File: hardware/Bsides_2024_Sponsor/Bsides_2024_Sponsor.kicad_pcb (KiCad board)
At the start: 2 copper layers, 139.6 x 139.6 mm, 65 parts, among them J1 Serial_IN, J2 Add_On, J3 OLED, J4 Serial_OUT, J5 Battery, J6 Battery, P1 USB_C_Plug_USB2.0, Q1 DMG3415U-7, SW1 ON, SW2 RESET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

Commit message: feat(hw): logos sponsor
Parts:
- added G***: LOGO, LOGO, B.Cu at (164.9, 141.1)
- added G***: LOGO, LOGO, B.Cu at (143.4, 102.8)
- added REF**: OSHW-Logo_7.5x8mm_SilkScreen, Symbol:OSHW-Logo_7.5x8mm_SilkScreen, B.Cu at (90.1, 132.8)
- added kibuzzard-666C8E87: G***, kibuzzard-666C8E87, B.Cu at (143.5, 98.5)
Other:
- board text added: "4e6576657220676f6e6e612067 69766520796f752075700a4e65 76657220676f6e6e61206c6574 20796f7520646f776e0a4e6576 657220676f6e6e612072756e20 61726f756e6420616e64206465 7365727420796f75"
- board text added: "Aqui inicia el tour por latinoamerica Parce Wey Che"
- board text added: "Elige tu bando, rudo o tecnico?"
- board text added: "Lucharan de 2 a 3 caidas sin limite de tiempo!!"

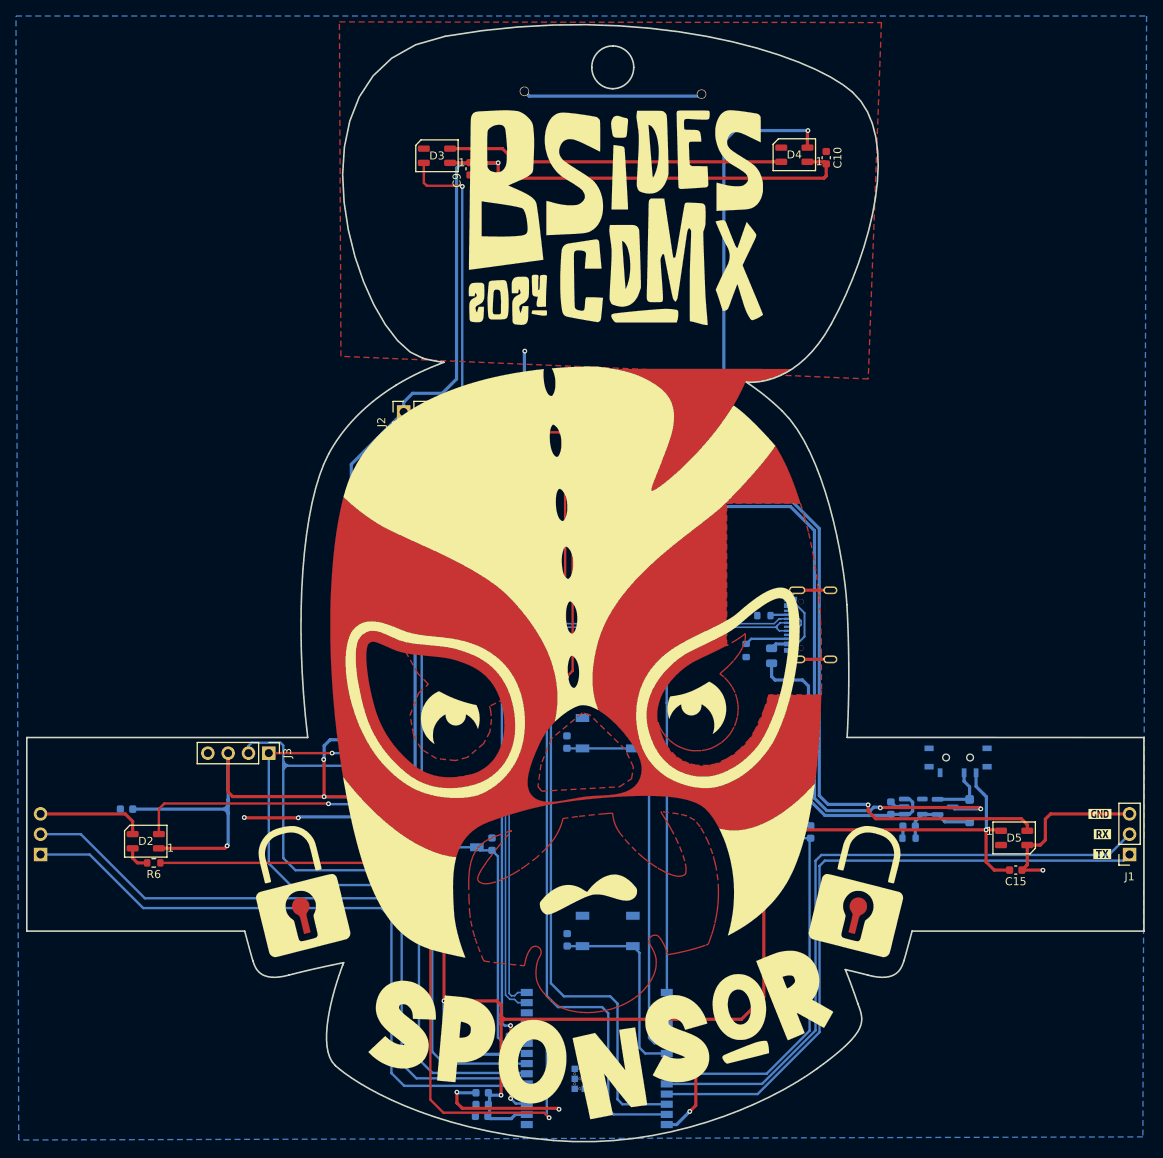
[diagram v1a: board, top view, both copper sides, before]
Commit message: feat(Hw):Update_footprint_badge
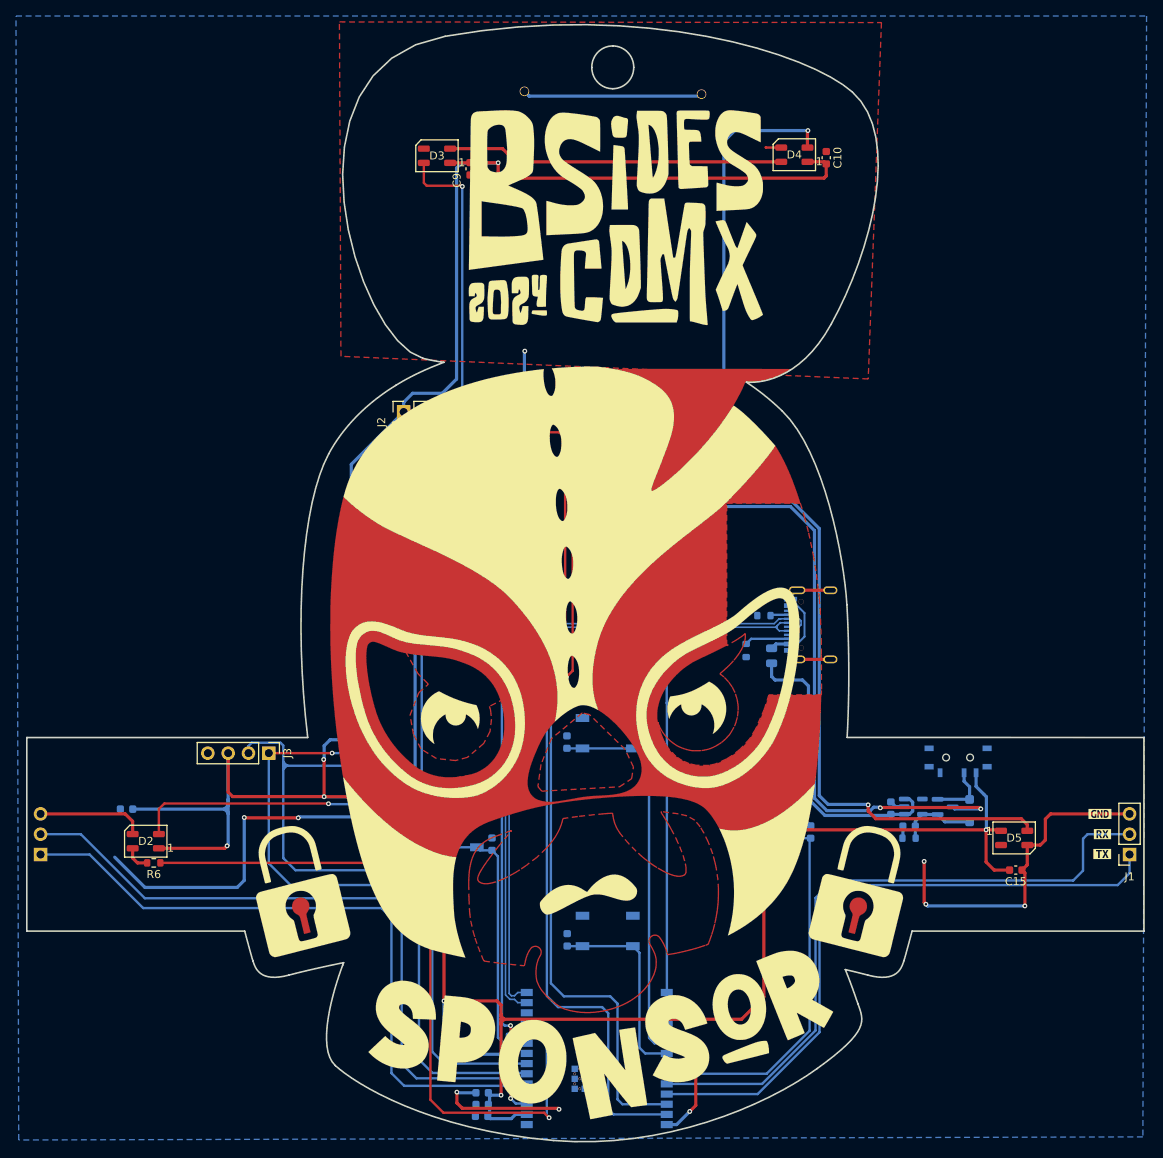
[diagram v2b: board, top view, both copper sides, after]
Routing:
- net GND: track 146.6 -> 194.4 mm, vias 10 -> 12
- net /TX: track 82.4 -> 81.3 mm

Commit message: feat(Hw): Update labels
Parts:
- removed kibuzzard-666B5C24: G***, kibuzzard-666B5C24
- removed kibuzzard-666B5C33: G***, kibuzzard-666B5C33
- added kibuzzard-666CA778: G***, kibuzzard-666CA778, B.Cu at (122.8, 76.5)
- added kibuzzard-666CA782: G***, kibuzzard-666CA782, B.Cu at (122.8, 68.2)
- moved REF** 2.00 mm to (88.9, 131.2)
